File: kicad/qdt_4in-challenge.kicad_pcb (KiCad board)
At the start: 2 copper layers, 84.1 x 61.7 mm, 46 parts, among them J1 Bus_PCI_Express_x1, J2 Conn_01x02, J3 MSD-4-A, J6 USB_C_Receptacle_USB2.0_16P, U2 RP2040, U4 W25Q128JVP, U9 MCP25625T-E/ML, X1 ABM8-272-T3, Y1 X322516MLB4SI

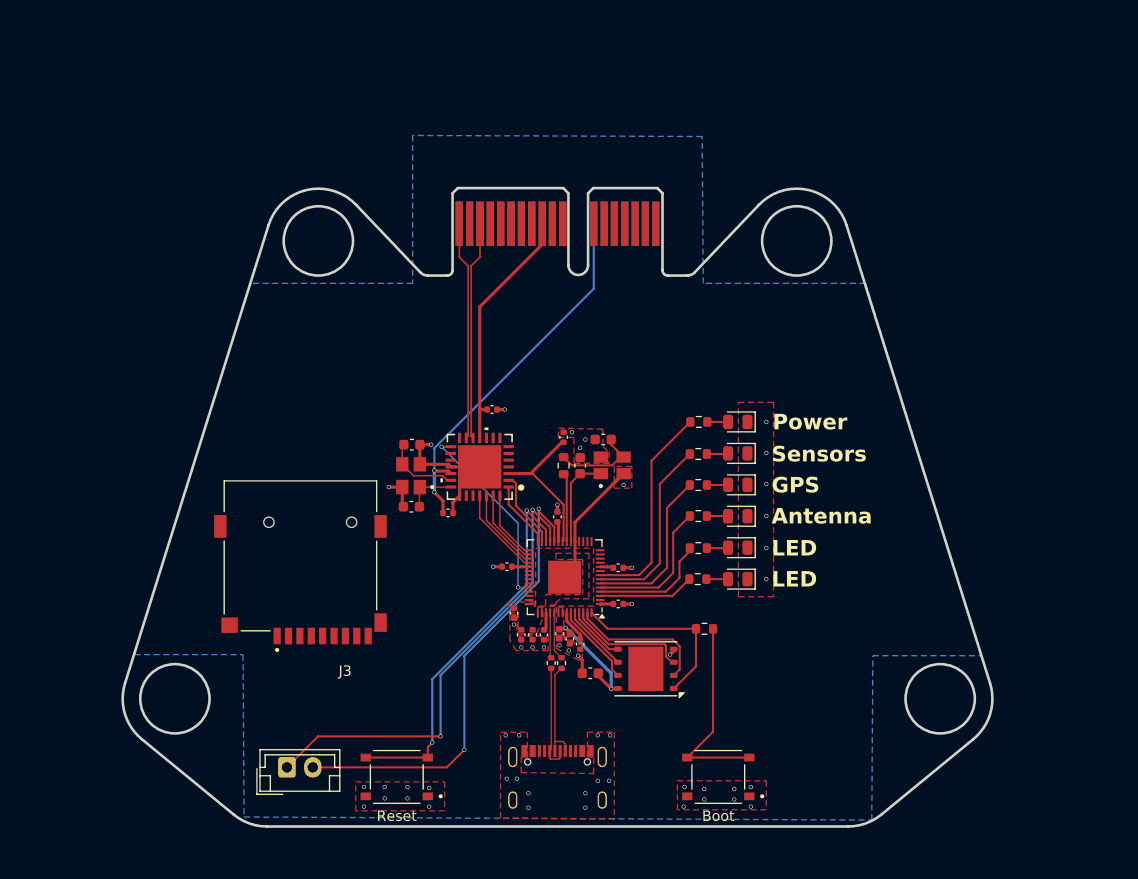
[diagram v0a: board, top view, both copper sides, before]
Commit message: Update file names and titles
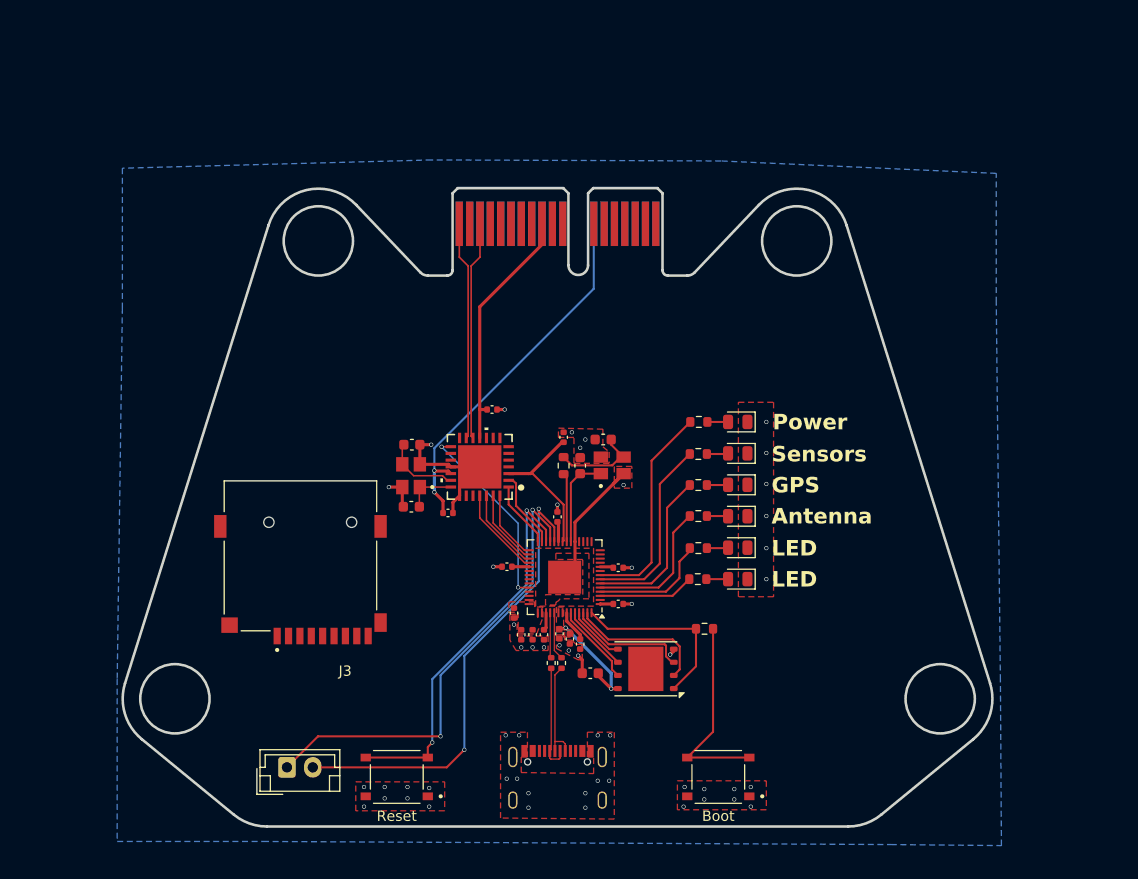
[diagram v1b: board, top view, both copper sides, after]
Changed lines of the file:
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@@
 		(polygon
 			(pts
-				(xy 132.4 69.9) (xy 116.7 69.9) (xy 105.5 105.8) (xy 116 105.8) (xy 116.1 121.5) (xy 176.8 121.8)
-				(xy 176.9 105.9) (xy 187.4 105.9) (xy 176.2 69.9) (xy 160.5 69.9) (xy 160.4 55.7) (xy 132.4 55.6)
+				(xy 104.333046 58.76549) (xy 104.333046 72.26549) (xy 103.833046 108.16549) (xy 103.833046 123.86549)
+				(xy 117.933046 123.86549) (xy 178.633046 124.16549) (xy 189.333046 124.26549) (xy 189.233046 108.26549)
+				(xy 188.833046 71.76549) (xy 188.833046 59.26549) (xy 162.233046 58.06549) (xy 134.233046 57.96549)
 			)
 		)

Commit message: Moved components and removed buttons from pcb
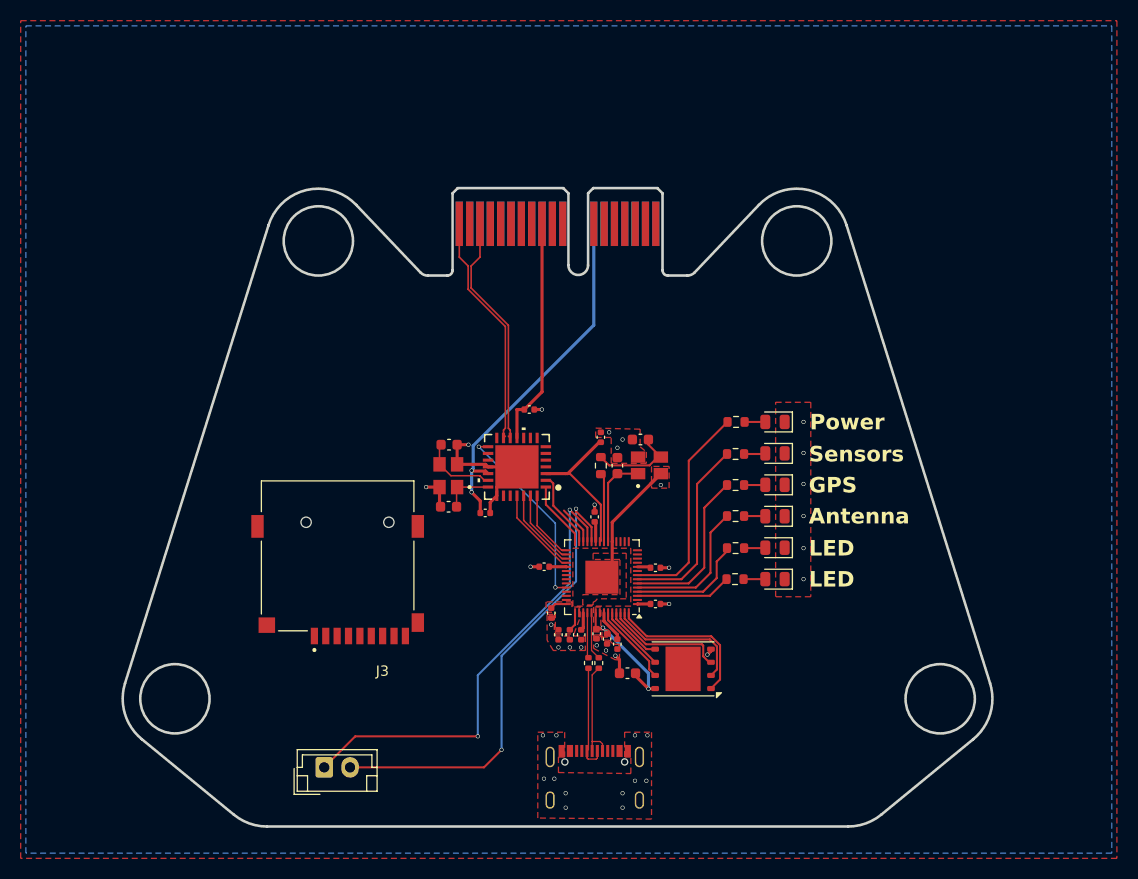
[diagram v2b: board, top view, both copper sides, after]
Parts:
- removed R4: 1k, Resistor_SMD:R_0603_1608Metric
- removed S1, S2: TS-1187A-B-A-B, TS-1187A-B-A-B:SW_TS-1187A-B-A-B
- moved C12 3.60 mm to (153.2, 107.6)
- moved C13 3.60 mm to (154.4, 85.0)
- moved C19 3.60 mm to (135.9, 85.5)
- moved C8 3.60 mm to (145.8, 101.8)
- moved R10 3.60 mm to (163.7, 83.3)
- moved U4 3.60 mm to (158.6, 107.2)
- moved X1 3.60 mm to (155.3, 87.5)
- moved J3 3.60 mm to (125.2, 96.2)
- moved C1 3.60 mm to (146.5, 103.9)
- moved C10 3.60 mm to (152.2, 104.8)
- moved C11 3.60 mm to (148.7, 103.9)
- moved C14 3.60 mm to (152.2, 87.5)
- moved C15 3.60 mm to (150.6, 84.8)
- moved C16 3.60 mm to (143.7, 82.1)
- moved C17 3.60 mm to (139.4, 92.1)
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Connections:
- U2 pad 26: /RUN -> unconnected-(U2-RUN-Pad26)
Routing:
- net /RUN: track 37.6 -> 0.00 mm, vias 2 -> 0
- net /~{USB_BOOT_S}: track 19.5 -> 0.00 mm
- net +5V: track 38.2 -> 43.0 mm
- net unconnected-(U2-RUN-Pad26): track 0.00 -> 3.78 mm
- net +3.3V: track 56.4 -> 59.7 mm
- net /QSPI_SS: track 17.4 -> 15.0 mm
- net CANP: track 22.9 -> 24.7 mm
- net CANN: track 22.9 -> 24.7 mm
- net GND: vias 53 -> 37
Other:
- board text removed: "Boot"
- board text removed: "Reset"
